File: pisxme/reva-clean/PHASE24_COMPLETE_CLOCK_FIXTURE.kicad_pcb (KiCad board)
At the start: 6 copper layers, 300 x 180 mm, 5 parts, among them U7 TUSB9261IPVP

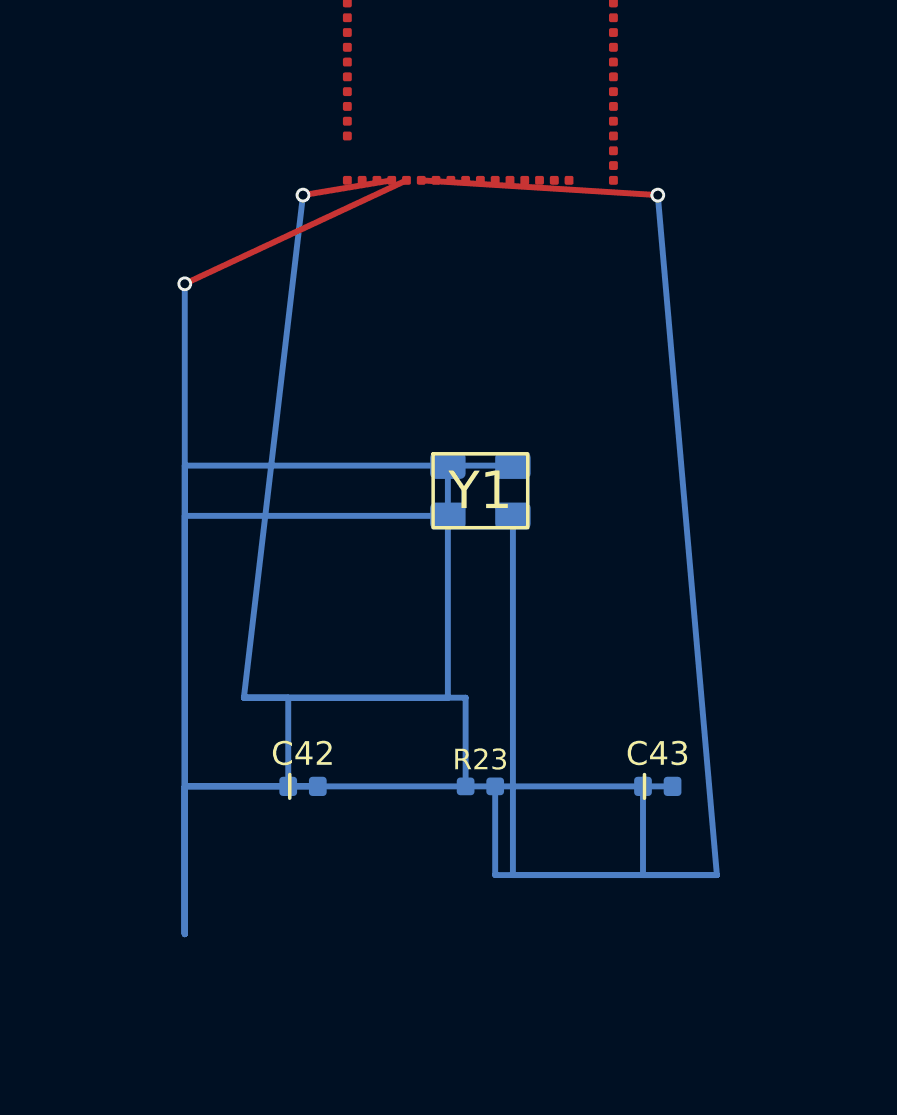
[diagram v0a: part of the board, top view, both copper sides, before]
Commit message: phase24 reject generic support bus
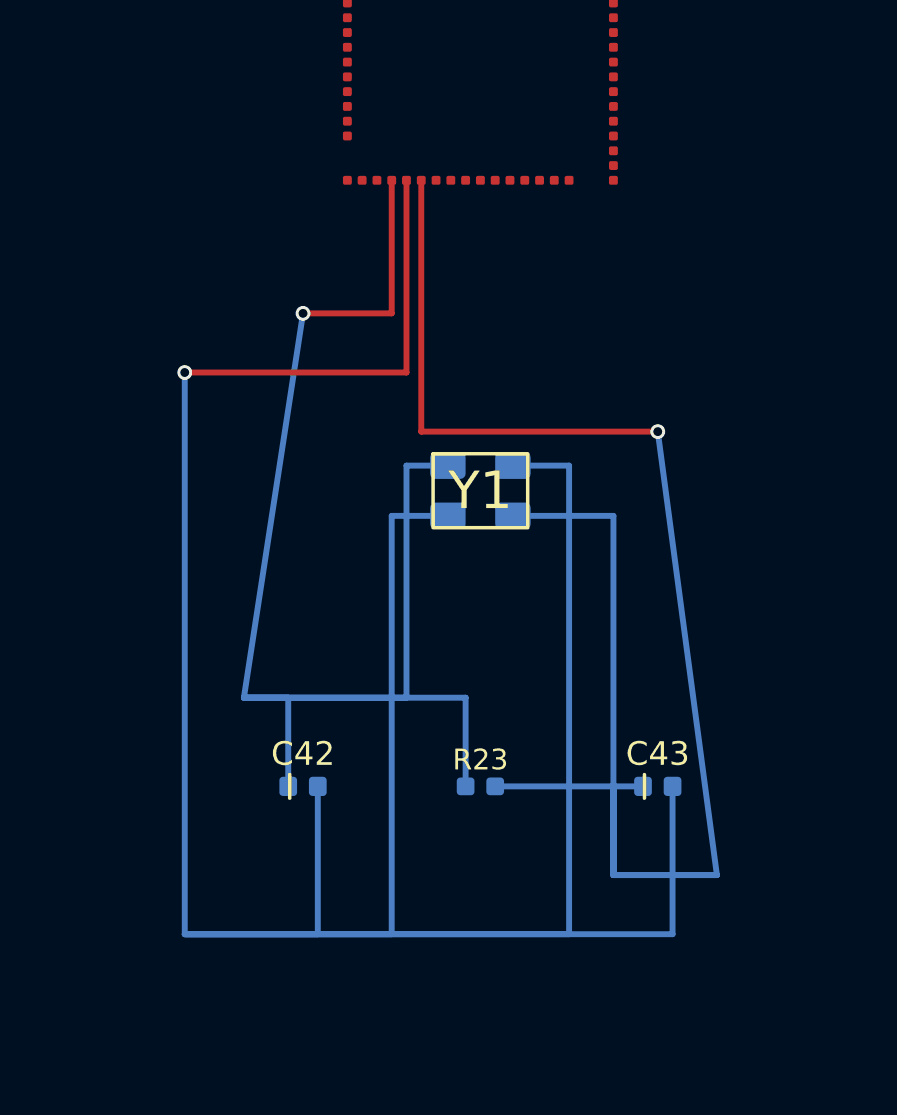
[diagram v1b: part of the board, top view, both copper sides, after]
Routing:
- net /STORAGE/BRIDGE_VSSOSC: track 111.3 -> 117.8 mm
- net /STORAGE/BRIDGE_XO: track 66.2 -> 68.7 mm
